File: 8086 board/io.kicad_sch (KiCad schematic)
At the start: 54 parts, among them J3 RGB LCD, U13 74AC573, U14 74AC573, U15 74AC573, U16 74AC573, U17 74LVC245A, U18 74LVC245A, U19 74LVC245A, U2 74HC32

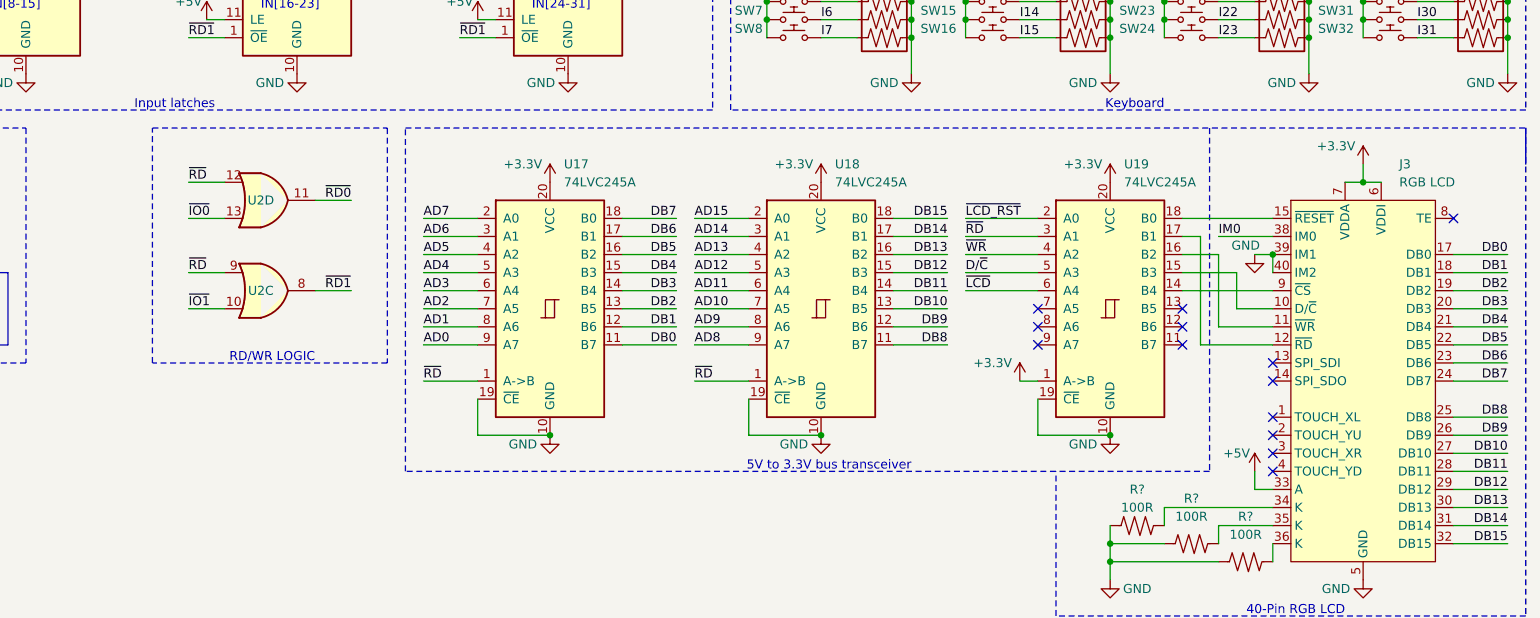
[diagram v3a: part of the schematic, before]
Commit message: PCB: different layout
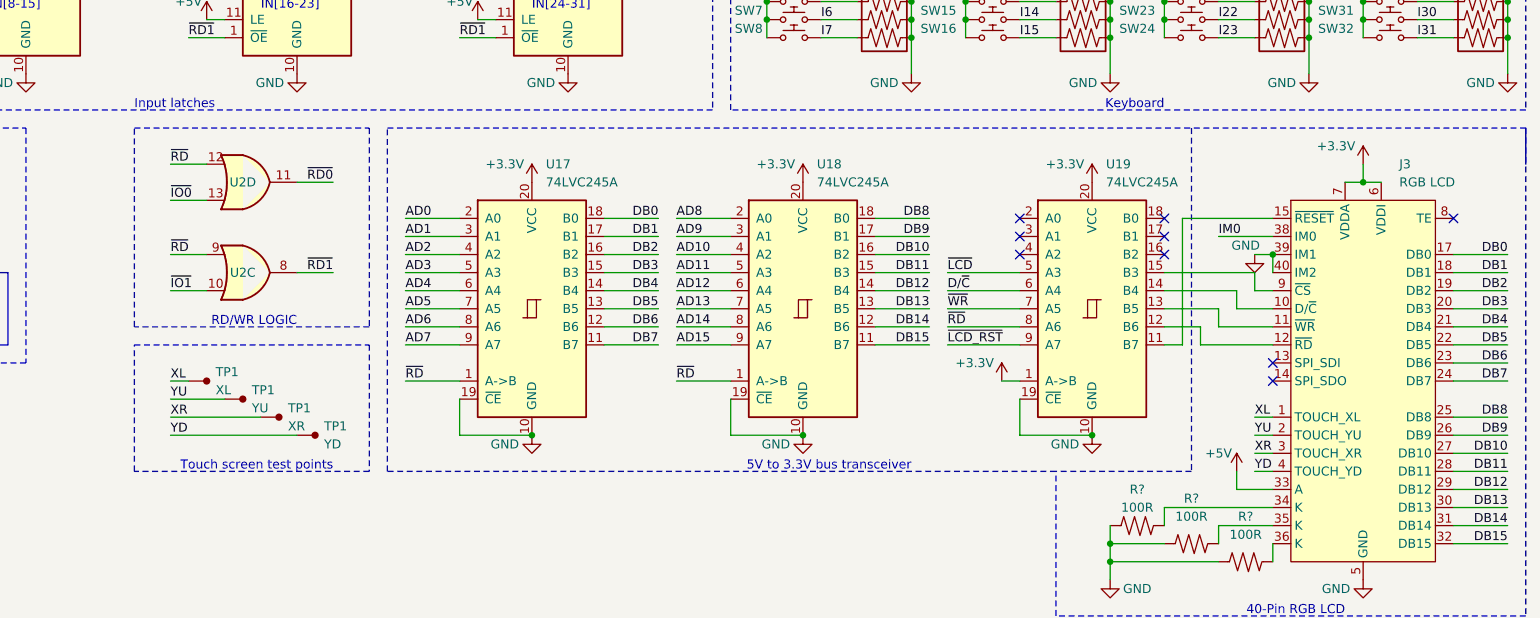
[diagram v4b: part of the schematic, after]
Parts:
- added TP1: XR, TestPoint:TestPoint_Pad_1.5x1.5mm, symbol 8086PC:TestPoint
- added TP1: XL, TestPoint:TestPoint_Pad_1.5x1.5mm, symbol 8086PC:TestPoint
- added TP1: YD, TestPoint:TestPoint_Pad_1.5x1.5mm, symbol 8086PC:TestPoint
- added TP1: YU, TestPoint:TestPoint_Pad_1.5x1.5mm, symbol 8086PC:TestPoint
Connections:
- net AD0: now also U17.2 (A0); no longer U17.9 (A7)
- net AD1: now also U17.3 (A1); no longer U17.8 (A6)
- net AD10: now also U18.4 (A2); no longer U18.7 (A5)
- net AD11: now also U18.5 (A3); no longer U18.6 (A4)
- net AD12: now also U18.6 (A4); no longer U18.5 (A3)
- net AD13: now also U18.7 (A5); no longer U18.4 (A2)
- net AD14: now also U18.8 (A6); no longer U18.3 (A1)
- net AD15: now also U18.9 (A7); no longer U18.2 (A0)
- net AD2: now also U17.4 (A2); no longer U17.7 (A5)
- net AD3: now also U17.5 (A3); no longer U17.6 (A4)
- net AD4: now also U17.6 (A4); no longer U17.5 (A3)
- net AD5: now also U17.7 (A5); no longer U17.4 (A2)
- net AD6: now also U17.8 (A6); no longer U17.3 (A1)
- net AD7: now also U17.9 (A7); no longer U17.2 (A0)
- net AD8: now also U18.2 (A0); no longer U18.9 (A7)
- net AD9: now also U18.3 (A1); no longer U18.8 (A6)
- net DB0: now also U17.18 (B0); no longer U17.11 (B7)
- net DB1: now also U17.17 (B1); no longer U17.12 (B6)
- net DB10: now also U18.16 (B2); no longer U18.13 (B5)
- net DB11: now also U18.15 (B3); no longer U18.14 (B4)
- net DB12: now also U18.14 (B4); no longer U18.15 (B3)
- net DB13: now also U18.13 (B5); no longer U18.16 (B2)
- net DB14: now also U18.12 (B6); no longer U18.17 (B1)
- net DB15: now also U18.11 (B7); no longer U18.18 (B0)
- net DB2: now also U17.16 (B2); no longer U17.13 (B5)
- net DB3: now also U17.15 (B3); no longer U17.14 (B4)
- net DB4: now also U17.14 (B4); no longer U17.15 (B3)
- net DB5: now also U17.13 (B5); no longer U17.16 (B2)
- net DB6: now also U17.12 (B6); no longer U17.17 (B1)
- net DB7: now also U17.11 (B7); no longer U17.18 (B0)
- net DB8: now also U18.18 (B0); no longer U18.11 (B7)
- net DB9: now also U18.17 (B1); no longer U18.12 (B6)
- net D/~{C}: now also U19.6 (A4); no longer U19.5 (A3)
- net ~{LCD_RST}: now also U19.9 (A7); no longer U19.2 (A0)
- net ~{LCD}: now also U19.5 (A3); no longer U19.6 (A4)
- net ~{RD}: now also U19.8 (A6); no longer U19.3 (A1)
- net ~{WR}: now also U19.7 (A5); no longer U19.4 (A2)
- net at U19.11 (B7): now also J3.15 (~{RESET})
- net at U19.12 (B6): now also J3.12 (~{RD})
- net at U19.13 (B5): now also J3.11 (~{WR})
- net at U19.14 (B4): now also J3.10 (D/~{C}); no longer J3.9 (~{CS})
- net at U19.15 (B3): now also J3.9 (~{CS}); no longer J3.10 (D/~{C})
- net at U19.16 (B2): no longer J3.11 (~{WR})
- net at U19.17 (B1): no longer J3.12 (~{RD})
- net at U19.18 (B0): no longer J3.15 (~{RESET})
- net XL: now reaches J3.1 (TOUCH_XL)
- net XL: now also TP1.1
- net YU: now reaches J3.2 (TOUCH_YU)
- net YU: now also TP1.1
- net XR: now reaches J3.3 (TOUCH_XR)
- net XR: now also TP1.1
- net YD: now reaches J3.4 (TOUCH_YD)
- net YD: now also TP1.1
- no-connect marks 14 -> 10
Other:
- note added: "Touch screen test points"
- moved on the sheet: U17, U18, U19, U2C, U2D

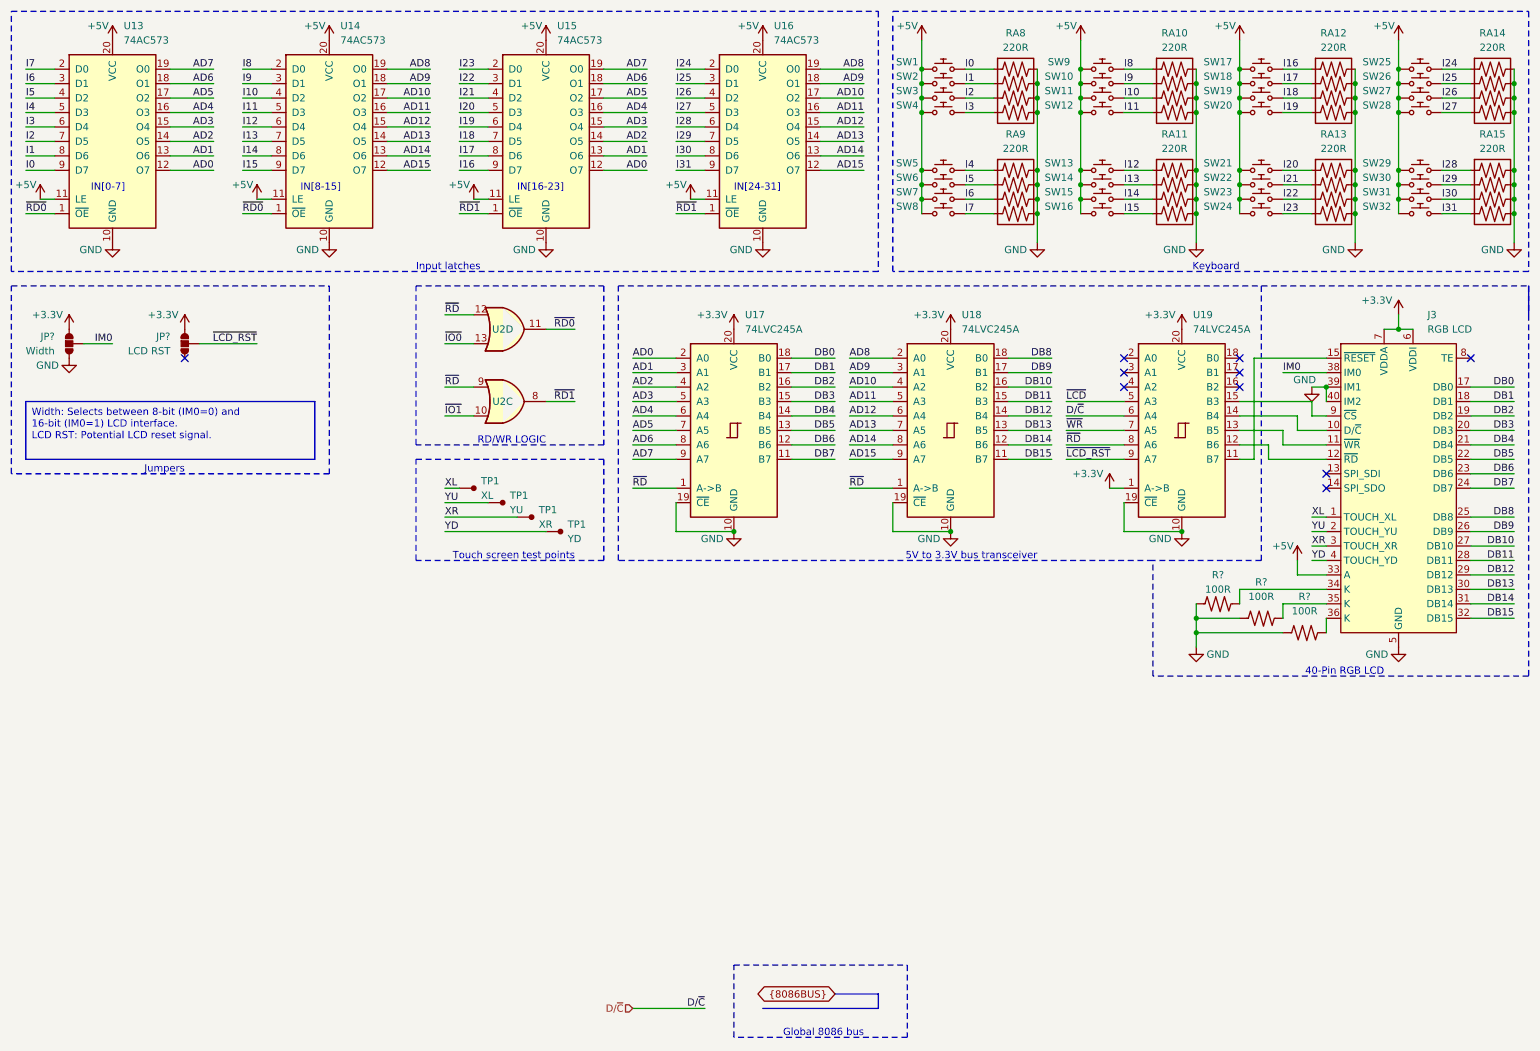
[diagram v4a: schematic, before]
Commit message: PCB: layout and routing of IO, shift registers, and MCU
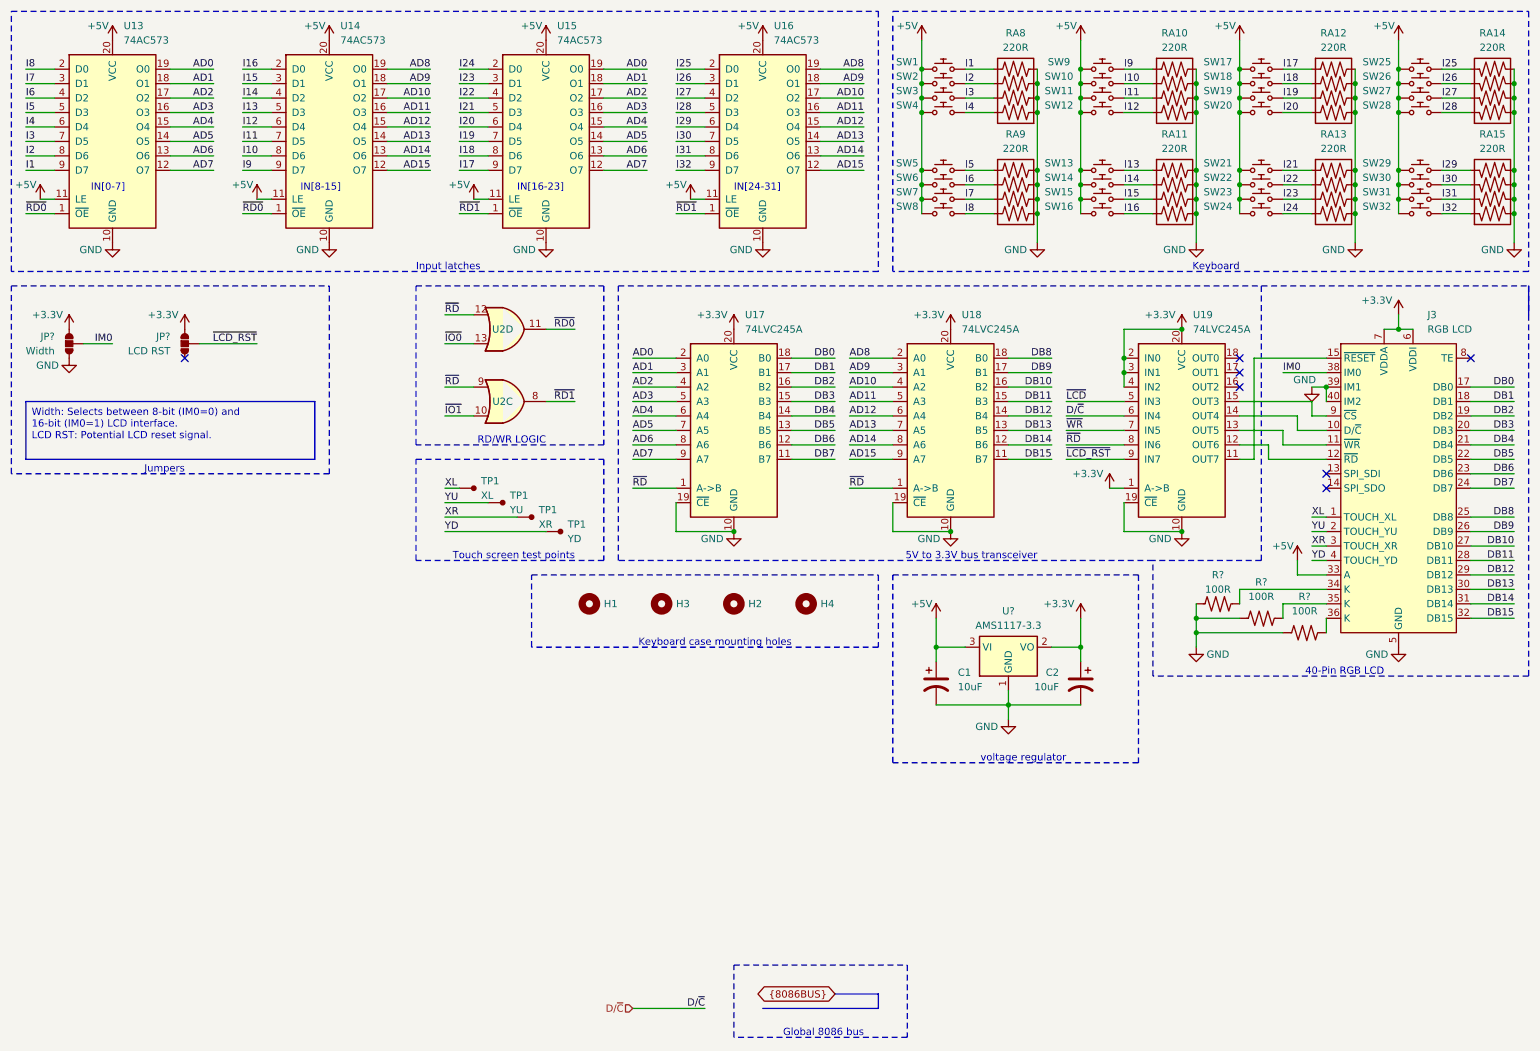
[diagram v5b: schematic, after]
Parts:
- added C1, C2: 10uF, Capacitor_SMD:C_0603_1608Metric_Pad1.08x0.95mm_HandSolder, symbol Device:C_Polarized_US
- added H1, H2, H3, H4: ~, MountingHole:MountingHole_3.2mm_M3_DIN965, symbol Mechanical:MountingHole
- added U?: AMS1117-3.3, Package_TO_SOT_SMD:SOT-223-3_TabPin2, symbol Regulator_Linear:AMS1117-3.3
- renumbered SW5 to SW1, SW7 to SW2, SW6 to SW3, SW8 to SW4, SW4 to SW5, SW3 to SW6, SW2 to SW7, SW1 to SW8
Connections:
- net +3.3V: now also U19.2 (A0), U19.3 (A1), U19.4 (A2), C2.1, U?.2 (VO)
- net +5V: now also SW10.2, SW12.2, SW14.2, SW16.2, SW18.2, SW2.2, SW21.2, SW26.2, SW28.2, SW30.2, SW32.2, SW4.2, SW6.2, SW8.2, C1.1, U?.3 (VI); no longer SW10.1, SW12.1, SW14.1, SW16.1, SW18.1, SW2.1, SW21.1, SW26.1, SW28.1, SW30.1, SW32.1, SW4.1, SW6.1, SW8.1
- net AD0: now also U13.19 (O0), U15.19 (O0); no longer U13.12 (O7), U15.12 (O7)
- net AD1: now also U13.18 (O1), U15.18 (O1); no longer U13.13 (O6), U15.13 (O6)
- net AD2: now also U13.17 (O2), U15.17 (O2); no longer U13.14 (O5), U15.14 (O5)
- net AD3: now also U13.16 (O3), U15.16 (O3); no longer U13.15 (O4), U15.15 (O4)
- net AD4: now also U13.15 (O4), U15.15 (O4); no longer U13.16 (O3), U15.16 (O3)
- net AD5: now also U13.14 (O5), U15.14 (O5); no longer U13.17 (O2), U15.17 (O2)
- net AD6: now also U13.13 (O6), U15.13 (O6); no longer U13.18 (O1), U15.18 (O1)
- net AD7: now also U13.12 (O7), U15.12 (O7); no longer U13.19 (O0), U15.19 (O0)
- net GND: now also RA8.1, RA8.2, RA8.3, RA8.4, RA9.1, RA9.2, RA9.3, RA9.4, C1.2, C2.2, U?.1 (GND); no longer RA8.5, RA8.6, RA8.7, RA8.8, RA9.5, RA9.6, RA9.7, RA9.8
- net I1: now also RA8.5, SW1.2, U13.9 (D7); no longer RA8.2, SW7.2, U13.8 (D6)
- net I10: now also RA10.2, SW10.1, U14.8 (D6); no longer RA10.3, SW11.2, U14.4 (D2)
- net I11: now also RA10.3, SW11.2, U14.7 (D5); no longer RA10.4, SW12.2, U14.5 (D3)
- net I12: now also RA10.4, SW12.1; no longer RA11.1, SW13.2
- net I13: now also RA11.1, SW13.2, U14.5 (D3); no longer RA11.2, SW14.2, U14.7 (D5)
- net I14: now also RA11.2, SW14.1, U14.4 (D2); no longer RA11.3, SW15.2, U14.8 (D6)
- net I15: now also RA11.3, SW15.2, U14.3 (D1); no longer RA11.4, SW16.2, U14.9 (D7)
- net I16: now also RA11.4, SW16.1, U14.2 (D0); no longer RA12.1, SW17.2, U15.9 (D7)
- net I17: now also RA12.1, SW17.2, U15.9 (D7); no longer RA12.2, SW18.2, U15.8 (D6)
- net I18: now also RA12.2, SW18.1, U15.8 (D6); no longer RA12.3, SW19.2, U15.7 (D5)
- net I19: now also RA12.3, SW19.2, U15.7 (D5); no longer RA12.4, SW20.2, U15.6 (D4)
- net I2: now also RA8.6, SW2.1, U13.8 (D6); no longer RA8.3, SW6.2, U13.7 (D5)
- net I20: now also RA12.4, SW20.2, U15.6 (D4); no longer RA13.1, SW21.2, U15.5 (D3)
- net I21: now also RA13.1, SW21.1, U15.5 (D3); no longer RA13.2, SW22.2, U15.4 (D2)
- net I22: now also RA13.2, SW22.2, U15.4 (D2); no longer RA13.3, SW23.2, U15.3 (D1)
- net I23: now also RA13.3, SW23.2, U15.3 (D1); no longer RA13.4, SW24.2, U15.2 (D0)
- net I24: now also RA13.4, SW24.2, U15.2 (D0); no longer RA14.1, SW25.2, U16.2 (D0)
- net I25: now also RA14.4, SW25.2, U16.2 (D0); no longer RA14.2, SW26.2, U16.3 (D1)
- net I26: now also SW26.1, U16.3 (D1); no longer SW27.2, U16.4 (D2)
- net I27: now also RA14.2, SW27.2, U16.4 (D2); no longer RA14.4, SW28.2, U16.5 (D3)
- net I28: now also RA14.1, SW28.1, U16.5 (D3); no longer RA15.1, SW29.2, U16.6 (D4)
- net I29: now also RA15.4, SW29.2, U16.6 (D4); no longer RA15.2, SW30.2, U16.7 (D5)
- net I3: now also RA8.7, SW3.2, U13.7 (D5); no longer RA8.4, SW5.2, U13.6 (D4)
- net I30: now also SW30.1, U16.7 (D5); no longer SW31.2, U16.8 (D6)
- net I31: now also RA15.2, SW31.2, U16.8 (D6); no longer RA15.4, SW32.2, U16.9 (D7)
- net I4: now also RA8.8, SW4.1, U13.6 (D4); no longer RA9.1, SW1.2, U13.5 (D3)
- net I5: now also RA9.5, SW5.2, U13.5 (D3); no longer RA9.2, SW3.2, U13.4 (D2)
- net I6: now also RA9.6, SW6.1, U13.4 (D2); no longer RA9.3, SW2.2, U13.3 (D1)
- net I7: now also RA9.7, SW7.2, U13.3 (D1); no longer RA9.4, SW4.2, U13.2 (D0)
- net I8: now also RA9.8, SW8.1, U13.2 (D0); no longer RA10.1, SW9.2, U14.2 (D0)
- net I9: now also RA10.1, SW9.2, U14.9 (D7); no longer RA10.2, SW10.2, U14.3 (D1)
- removed net I0: RA8.1, SW8.2, U13.9 (D7)
- new net I32: RA15.1, SW32.1, U16.9 (D7)
- no-connect marks 10 -> 7
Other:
- note added: "Keyboard case mounting holes"
- note added: "voltage regulator"
- moved on the sheet: RA8, RA9, SW1, SW2, SW3, SW4, SW5, SW6, SW7, SW8

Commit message: small schematic  changes to better fit PCB
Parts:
- removed H4: ~, MountingHole:MountingHole_3.2mm_M3_DIN965, symbol Mechanical:MountingHole
- RA10, RA11, RA12, RA13, RA14, RA15, RA8, RA9: value 220R -> 10k
- SW1: value ~ -> Q
- SW10: value ~ -> A
- SW11: value ~ -> S
- SW12: value ~ -> D
- SW13: value ~ -> F
- SW14: value ~ -> G
- SW15: value ~ -> H
- SW16: value ~ -> J
- SW17: value ~ -> O
- SW18: value ~ -> P
- SW19: value ~ -> Backspace
- SW2: value ~ -> W
- SW20: value ~ -> K
- SW21: value ~ -> L
- SW22: value ~ -> enter
- SW23: value ~ -> M
- SW24: value ~ -> space
- SW25: value ~ -> alt
- SW26: value ~ -> ctrl
- SW27: value ~ -> Z
- SW28: value ~ -> X
- SW29: value ~ -> C
- SW3: value ~ -> E
- SW30: value ~ -> V
- SW31: value ~ -> B
- SW32: value ~ -> N
- SW4: value ~ -> R
- SW5: value ~ -> T
- SW6: value ~ -> Y
- SW7: value ~ -> U
- SW8: value ~ -> I
- SW9: value ~ -> shift
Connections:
- net ~{IO0}: now also U2.10; no longer U2.13
- net ~{IO1}: now also U2.13; no longer U2.10
- net ~{RD0}: now also U2.8; no longer U2.11
- net ~{RD1}: now also U2.11; no longer U2.8
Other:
- moved on the sheet: H1, H2, H3

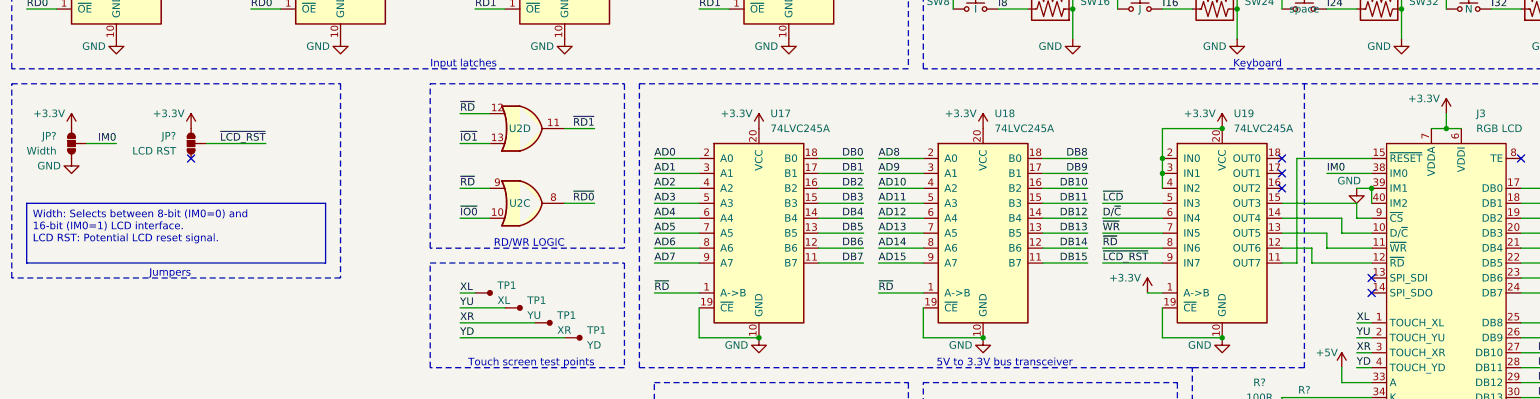
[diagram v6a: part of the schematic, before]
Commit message: remove LCD reset jumper
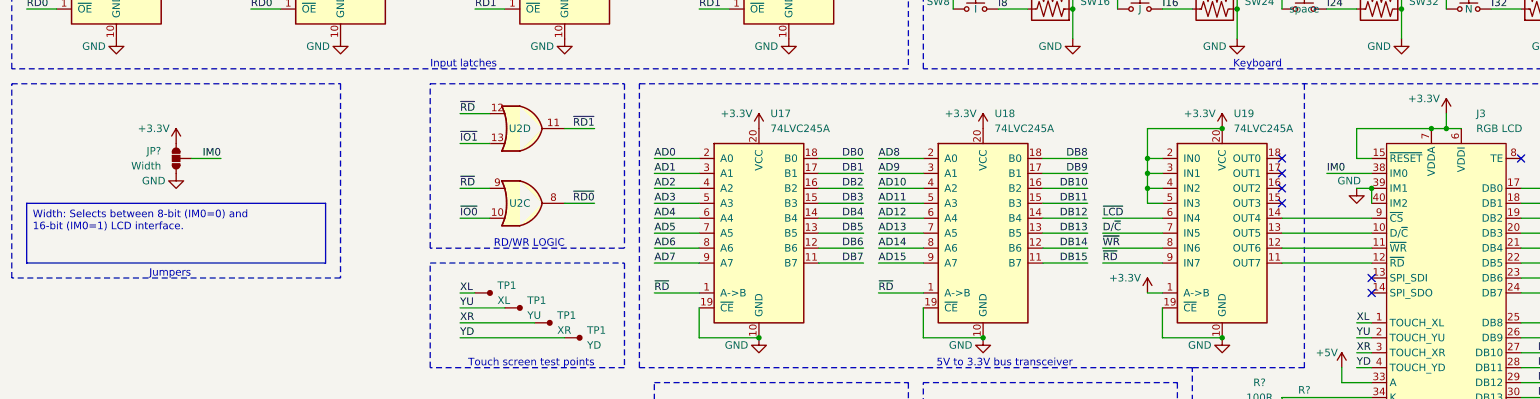
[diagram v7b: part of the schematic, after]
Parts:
- removed JP?: LCD RST, Jumper:SolderJumper-3_P1.3mm_Bridged12_RoundedPad1.0x1.5mm, symbol 8086PC:SolderJumper
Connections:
- net ~{LCD_RST} is gone; now on net ~{RD}: U19.9 (A7)
- net +3.3V: now also J3.15 (~{RESET}), U19.5 (A3)
- net D/~{C}: now also U19.7 (A5); no longer U19.6 (A4)
- net ~{LCD}: now also U19.6 (A4); no longer U19.5 (A3)
- net ~{RD}: no longer U19.8 (A6)
- net ~{WR}: now also U19.8 (A6); no longer U19.7 (A5)
- net at U19.11 (B7): now also J3.12 (~{RD}); no longer J3.15 (~{RESET})
- net at U19.12 (B6): now also J3.11 (~{WR}); no longer J3.12 (~{RD})
- net at U19.13 (B5): now also J3.10 (D/~{C}); no longer J3.11 (~{WR})
- net at U19.14 (B4): now also J3.9 (~{CS}); no longer J3.10 (D/~{C})
- net at U19.15 (B3): no longer J3.9 (~{CS})
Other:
- moved on the sheet: JP?
